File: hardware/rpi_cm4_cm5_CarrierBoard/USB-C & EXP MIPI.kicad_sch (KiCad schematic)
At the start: 16 parts, among them J16 12401598E4#2A, J17 5051102291, U23 AP22913W6-7

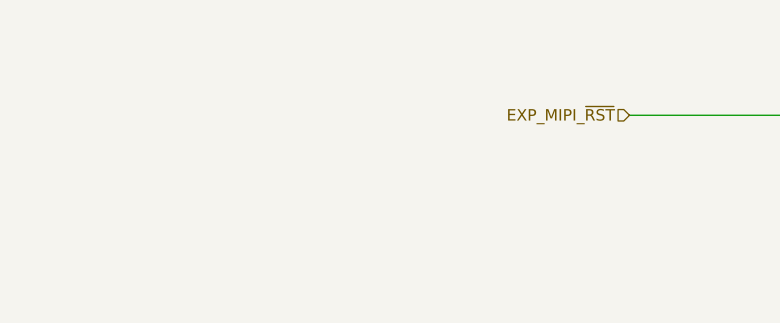
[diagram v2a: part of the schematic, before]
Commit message: Update schematic sheets (assembly variants, default cap / res notes)
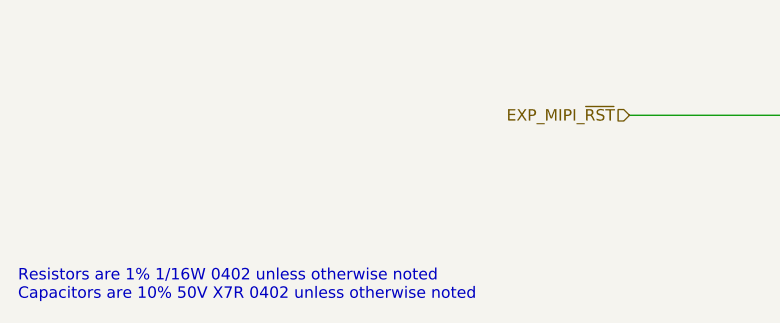
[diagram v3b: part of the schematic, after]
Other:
- note added: "Resistors are 1% 1/16W 0402 unless otherwise noted Capacitors are 10% 50V X7R 0402 unless otherwise noted"
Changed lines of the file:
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@@
 	(title_block
 		(title "RPI CMx Carrier")
-		(date "2026-02-20")
+		(date "2026-02-22")
 		(rev "2.00-0A")
 		(comment 1 "Jean-Francois Bilodeau")
@@
 		(comment 9 "RPI_CMx_Carrier_2.00-0A_BOM")
 	)
+	(text "Resistors are 1% 1/16W 0402 unless otherwise noted\nCapacitors are 10% 50V X7R 0402 unless otherwise noted"
+		(exclude_from_sim no)
+		(at 12.7 170.688 0)
+		(effects
+			(font
+				(size 1.27 1.27)
+			)
+			(justify left)
+		)
+	)
 	(junction
